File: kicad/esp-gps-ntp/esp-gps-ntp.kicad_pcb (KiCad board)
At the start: 2 copper layers, 60 x 100 mm, 26 parts, among them J1 Power, J2 Serial, J3 JTAG, J4 Display, J5 GPS, J6 UltimateGPS, SW1 Reset, U1 MCP1825-3302E, U2 ESP32-WROOM-32D, U3 DS3231M

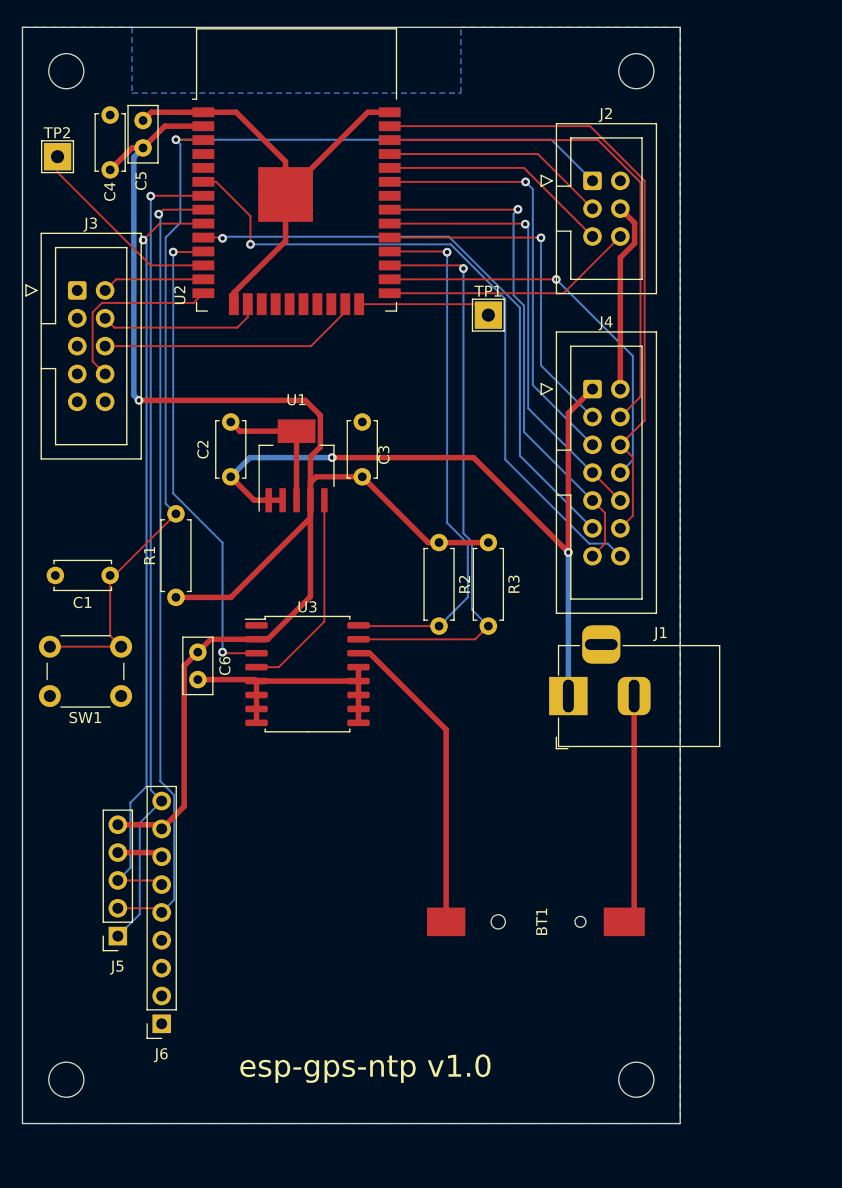
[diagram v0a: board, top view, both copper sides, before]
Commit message: new board version fix idle time hack
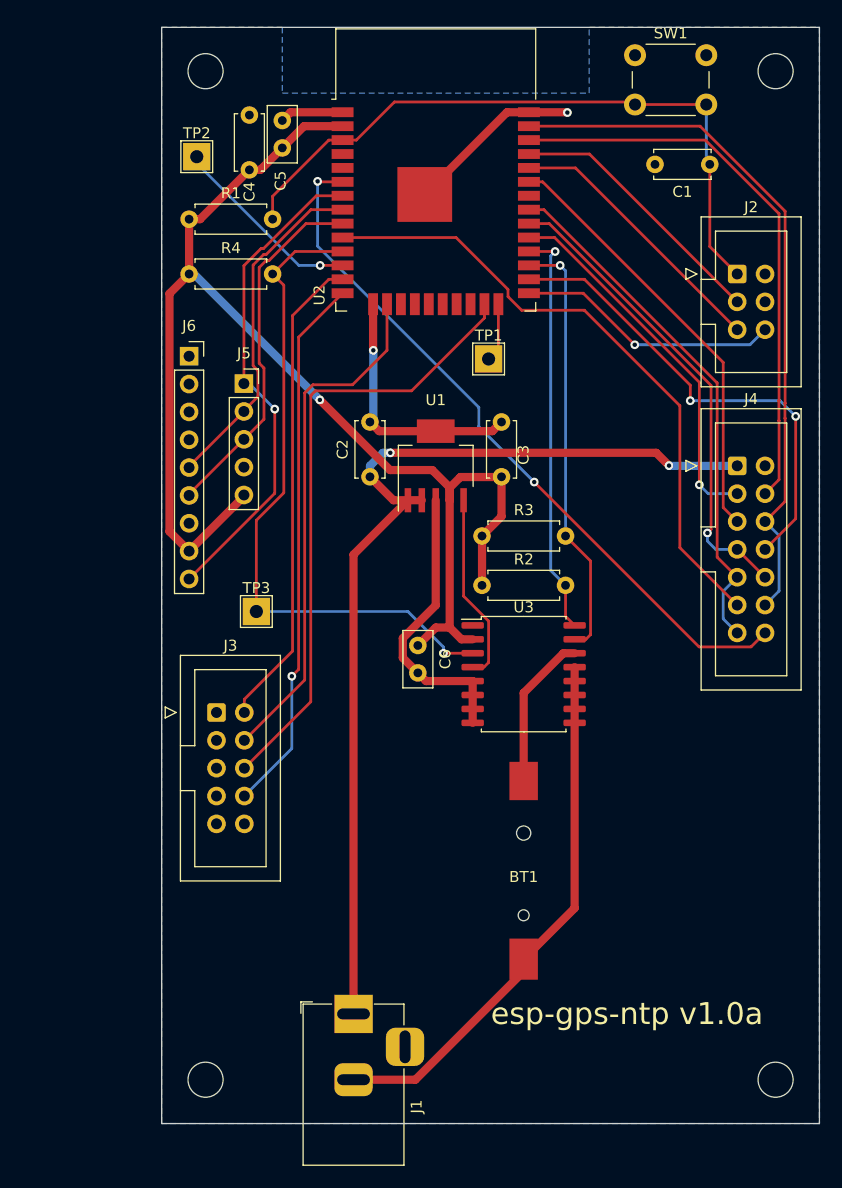
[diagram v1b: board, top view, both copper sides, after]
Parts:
- added R4: 10k, Resistor_THT:R_Axial_DIN0207_L6.3mm_D2.5mm_P7.62mm_Horizontal, F.Cu at (115.2, 92.5)
- added TP3: SQW, TestPoint:TestPoint_THTPad_2.5x2.5mm_Drill1.2mm, F.Cu at (121.3, 123.3)
- moved SW1 74.9 mm to (155.9, 72.5), turned to 0 degrees
- moved C1 66.3 mm to (162.7, 82.5)
- moved J6 61.0 mm to (115.2, 100.0), turned to 0 degrees
- moved J5 51.7 mm to (120.2, 102.5), turned to 0 degrees
- moved J3 40.5 mm to (117.7, 132.5)
- moved J1 35.0 mm to (130.2, 160.0), turned to 90 degrees
- moved R1 34.5 mm to (115.2, 87.5), turned to 0 degrees
- moved C6 20.1 mm to (136.1, 126.4)
- moved U3 19.7 mm to (145.7, 129.0)
- moved J2 15.7 mm to (165.2, 92.5)
- moved J4 14.9 mm to (165.2, 110.0)
- moved C4 12.7 mm to (120.7, 83.0)
- moved C5 12.7 mm to (123.7, 81.0)
- moved H1 12.7 mm to (116.7, 74.0)
- moved H3 12.7 mm to (116.7, 166.0)
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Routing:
- net /GPS_TXD: track 73.1 -> 31.5 mm, vias 1 -> 0
- net /GPS_RXD: track 70.0 -> 33.1 mm, vias 1 -> 0
- net /RST: track 99.0 -> 62.4 mm, vias 1 -> 0
- net /TMS: track 9.38 -> 44.0 mm
- net /TDI: track 16.9 -> 49.6 mm, vias 0 -> 1
- net /TDO: track 23.9 -> 56.5 mm
- net /TCK: track 14.9 -> 47.3 mm
- net /GPS_PPS: track 74.4 -> 44.9 mm
- net +5V: track 69.6 -> 90.0 mm
- net /SQW: track 44.3 -> 61.1 mm, vias 2 -> 1
- net +3V3: track 140.3 -> 124.1 mm
- net /BATT: track 28.4 -> 14.2 mm
- net /SDA: track 52.8 -> 39.3 mm
- net /SCL: track 48.6 -> 37.6 mm
- net /TFT_LED: track 36.2 -> 43.6 mm, vias 1 -> 2
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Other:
- net class Default: clearance 0.2 -> 0.3; trace_width 0.1778 -> 0.254
- net class Power: trace_width 0.5 -> 0.75
- rule trace_clearance: 0.2 -> 0.3
- board text added: "esp-gps-ntp v1.0a"
- board text removed: "esp-gps-ntp v1.0"
